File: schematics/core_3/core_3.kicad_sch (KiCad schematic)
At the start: 14 parts

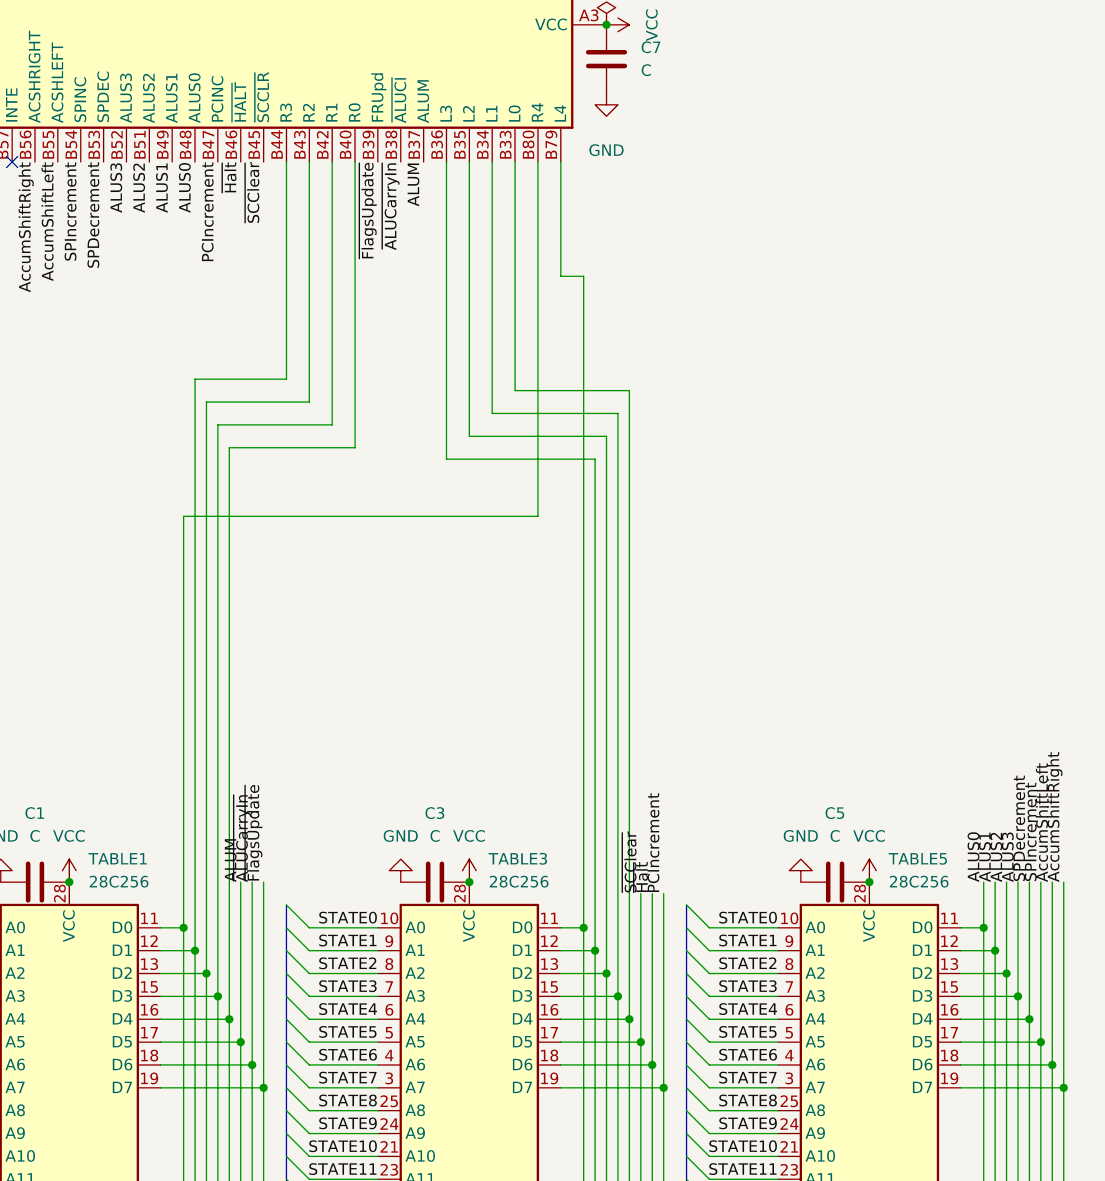
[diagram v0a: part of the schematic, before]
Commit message: Add pcb for core 3
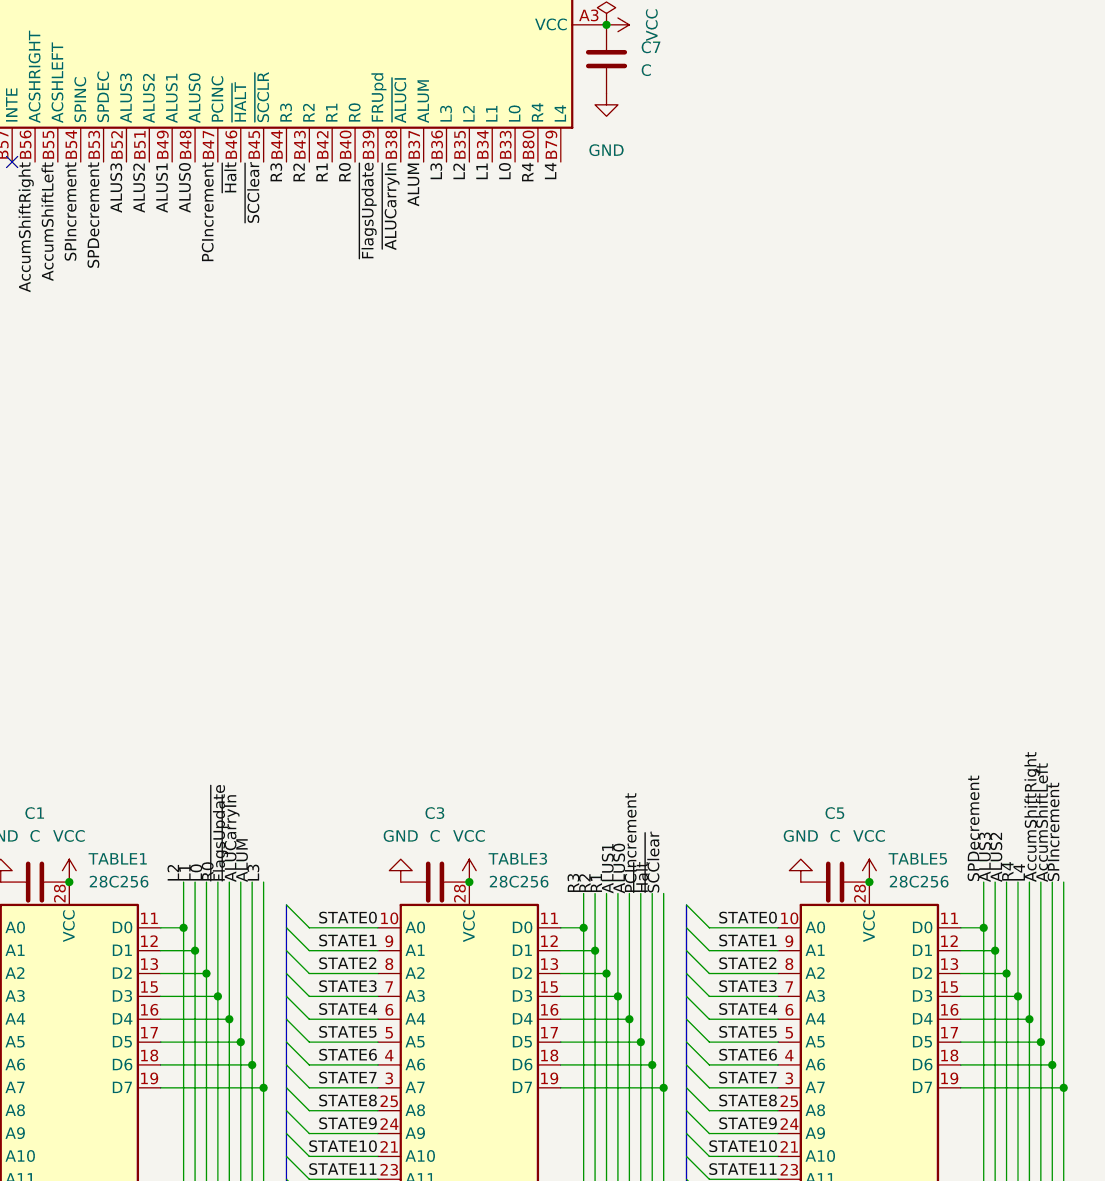
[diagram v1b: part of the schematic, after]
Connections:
- net ALUM: now also TABLE1.18 (D6), TABLE2.18 (D6); no longer TABLE1.17 (D5), TABLE2.17 (D5)
- net ALUS0: now also TABLE3.16 (D4), TABLE4.16 (D4); no longer TABLE5.11 (D0), TABLE6.11 (D0)
- net ALUS1: now also TABLE3.15 (D3), TABLE4.15 (D3); no longer TABLE5.12 (D1), TABLE6.12 (D1)
- net ALUS3: now also TABLE5.12 (D1), TABLE6.12 (D1); no longer TABLE5.15 (D3), TABLE6.15 (D3)
- net AccumShiftRight: now also TABLE5.17 (D5), TABLE6.17 (D5); no longer TABLE5.19 (D7), TABLE6.19 (D7)
- net GND: no longer BC2.A41 (GND), BC2.B41 (GND)
- net PCIncrement: now also TABLE3.17 (D5), TABLE4.17 (D5); no longer TABLE3.19 (D7), TABLE4.19 (D7)
- net SPDecrement: now also TABLE5.11 (D0), TABLE6.11 (D0); no longer TABLE5.16 (D4), TABLE6.16 (D4)
- net SPIncrement: now also TABLE5.19 (D7), TABLE6.19 (D7); no longer TABLE5.17 (D5), TABLE6.17 (D5)
- net ~{ALUCarryIn}: now also TABLE1.17 (D5), TABLE2.17 (D5); no longer TABLE1.18 (D6), TABLE2.18 (D6)
- net ~{FlagsUpdate}: now also TABLE1.16 (D4), TABLE2.16 (D4); no longer TABLE1.19 (D7), TABLE2.19 (D7)
- net ~{SCClear}: now also TABLE3.19 (D7), TABLE4.19 (D7); no longer TABLE3.17 (D5), TABLE4.17 (D5)
- net R3: now reaches TABLE3.11 (D0), TABLE4.11 (D0)
- net R3: now also BC2.B44 (R3); no longer BC2.B79 (L4)
- net R2: now reaches TABLE3.12 (D1), TABLE4.12 (D1)
- net R2: now also BC2.B43 (R2); no longer BC2.B36 (L3)
- net R1: now reaches TABLE3.13 (D2), TABLE4.13 (D2)
- net R1: now also BC2.B42 (R1); no longer BC2.B35 (L2)
- net R0: now reaches TABLE1.15 (D3), TABLE2.15 (D3)
- net R0: now also BC2.B40 (R0); no longer BC2.B42 (R1)
- net L0: now reaches TABLE1.13 (D2), TABLE2.13 (D2)
- net L0: now also BC2.B33 (L0); no longer BC2.B43 (R2)
- net L1: now reaches TABLE1.12 (D1), TABLE2.12 (D1)
- net L1: now also BC2.B34 (L1); no longer BC2.B44 (R3)
- net L2: now reaches TABLE1.11 (D0), TABLE2.11 (D0)
- net L2: now also BC2.B35 (L2); no longer BC2.B80 (R4)
- new net L3: BC2.B36 (L3), TABLE1.19 (D7), TABLE2.19 (D7)
- new net L4: BC2.B79 (L4), TABLE5.16 (D4), TABLE6.16 (D4)
- new net R4: BC2.B80 (R4), TABLE5.15 (D3), TABLE6.15 (D3)

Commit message: Push periphery and fix schematics
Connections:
- net GND: no longer TABLE1.27 (~{WE}), TABLE2.27 (~{WE}), TABLE3.27 (~{WE}), TABLE4.27 (~{WE}), TABLE5.27 (~{WE}), TABLE6.27 (~{WE})
- net VCC: now also TABLE1.27 (~{WE}), TABLE2.27 (~{WE}), TABLE3.27 (~{WE}), TABLE4.27 (~{WE}), TABLE5.27 (~{WE}), TABLE6.27 (~{WE})
